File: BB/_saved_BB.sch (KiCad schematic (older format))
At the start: 234 parts, among them SW0 SW_Push, U1 AT90USB1286-AU, Y0 16Mhz

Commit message: Rows Done
Main Columns
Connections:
- net COL4: no longer MX67.3 (LED)
- net COL9: now also MX89.1 (COL)
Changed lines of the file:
@@
 $EndComp
 Wire Wire Line
-	8570 7010 8570 5680
+	8570 7010 8570 5735
+Wire Wire Line
+	8570 5735 8695 5735
+Wire Wire Line
+	8695 5735 8695 5540
+Wire Wire Line
+	8695 5540 8570 5540
+Wire Wire Line
+	8570 5540 8570 4285
 Connection ~ 8570 4285
-Connection ~ 8570 5680
 Wire Wire Line
-	8570 5680 8570 4285
+	9790 6320 9785 6320
 $EndSCHEMATC

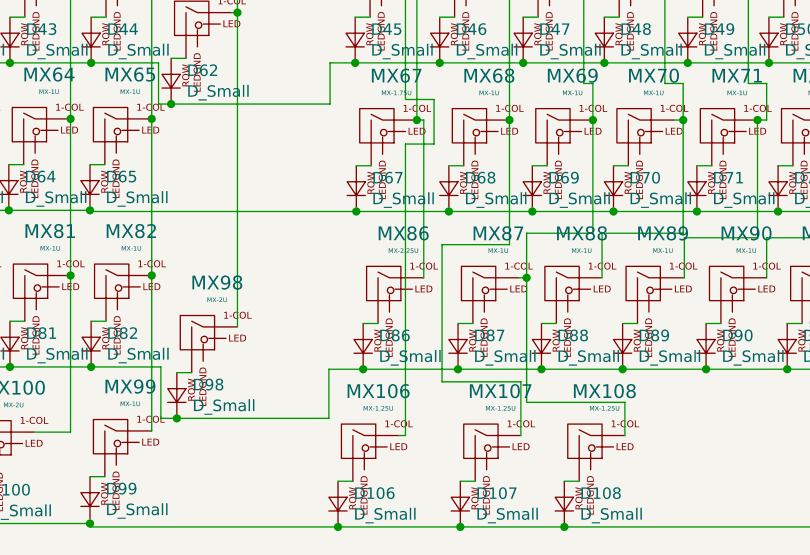
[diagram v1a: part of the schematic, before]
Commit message: MCU Wired
No rows or colomns
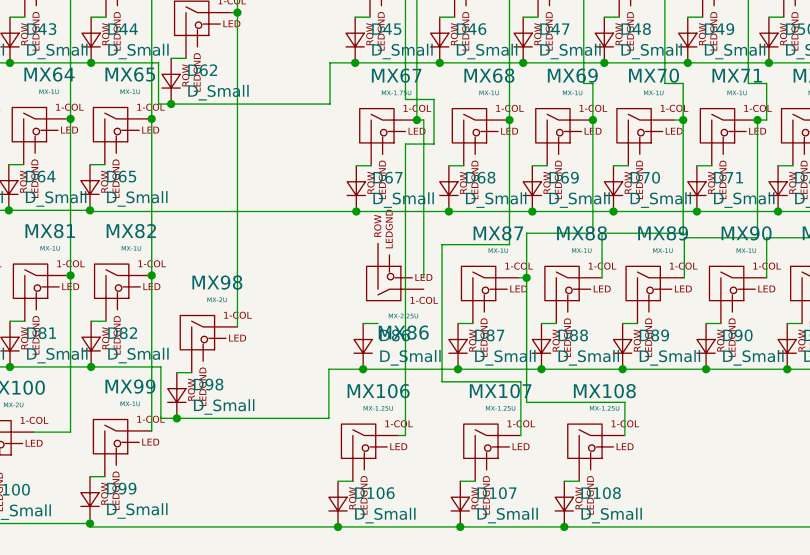
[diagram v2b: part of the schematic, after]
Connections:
- net COL5: no longer MX86.1 (COL)
- net at MX86.2 (ROW): no longer D86.2 (A)
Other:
- moved on the sheet: MX86
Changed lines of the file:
@@
 F 3 "" H 8450 6320 60  0001 C CNN
 	1    8475 6345
-	1    0    0    -1
+	1    0    0    1
 $EndComp
 $Comp
@@
 Wire Wire Line
 	4085 2025 4085 2110
-$Comp
-L MCU_Microchip_AVR:AT90USB1286-AU U1
-U 1 1 5CAEA573
-P 4185 4110
-F 0 "U1" H 4185 2021 50  0000 C CNN
-F 1 "AT90USB1286-AU" H 4185 1930 50  0000 C CNN
-F 2 "Package_QFP:TQFP-64_14x14mm_P0.8mm" H 4185 4110 50  0001 C CIN
-F 3 "http://ww1.microchip.com/downloads/en/DeviceDoc/doc7593.pdf" H 4185 4110 50  0001 C CNN
-	1    4185 4110
-	1    0    0    -1
-$EndComp
 Text GLabel 4785 4410 2    50   Input ~ 0
 COL0
@@
 Wire Wire Line
 	9790 6320 9785 6320
+$Comp
+L MCU_Microchip_AVR:AT90USB1286-AU U1
+U 1 1 5CAEA573
+P 4185 4110
+F 0 "U1" H 4185 2021 50  0000 C CNN
+F 1 "AT90USB1286-AU" H 4185 1930 50  0000 C CNN
+F 2 "Package_QFP:TQFP-64_14x14mm_P0.8mm" H 4185 4110 50  0001 C CIN
+F 3 "http://ww1.microchip.com/downloads/en/DeviceDoc/doc7593.pdf" H 4185 4110 50  0001 C CNN
+	1    4185 4110
+	1    0    0    -1
+$EndComp
 $EndSCHEMATC
